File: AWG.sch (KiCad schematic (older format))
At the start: 83 parts, among them J1001 Conn_01x03, J1002 Conn_01x05, J1003 Conn_01x06, J1004 Conn_01x06, J2 Conn afficheur, J5 SMA, J6 SMA, J7 BNC, Q1001 NTE2633, Q1002 NTE2634, SW1 Reset, SW2 Encodeur sur façade, SW3 Next, SW4 Previous, SW5 AC/DC, SW6 50R/Low Z, U1 Pico, U1001 LM7812, U1002 L7912, U1003 LM7805, U1004 LM7905, U3 AD8055ARZ

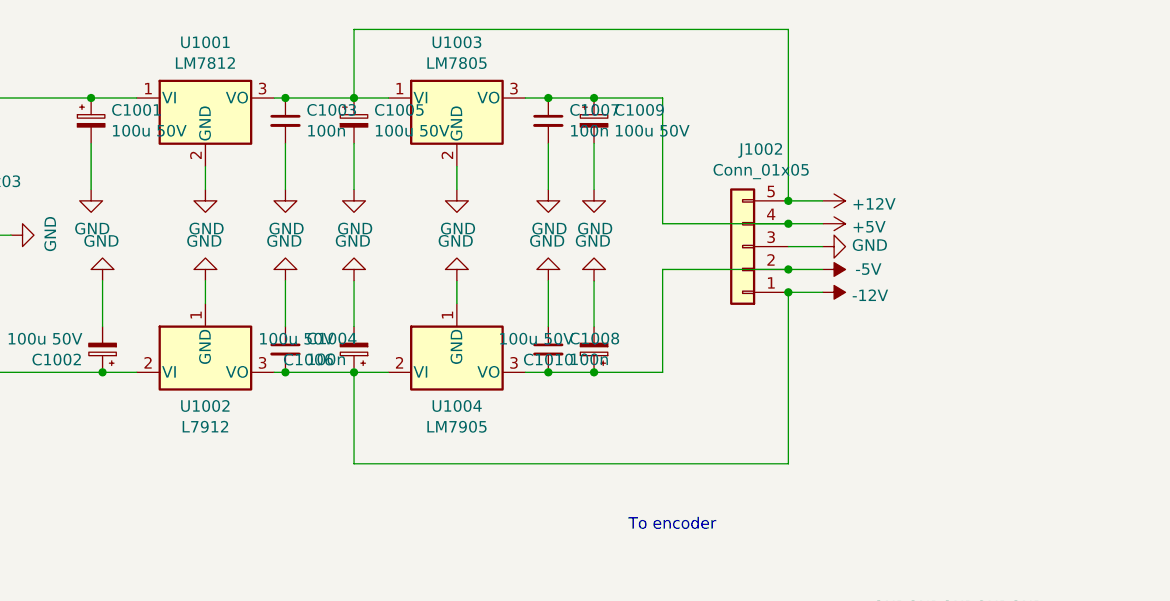
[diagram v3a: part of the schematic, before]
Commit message: D2Pack linear regulator added
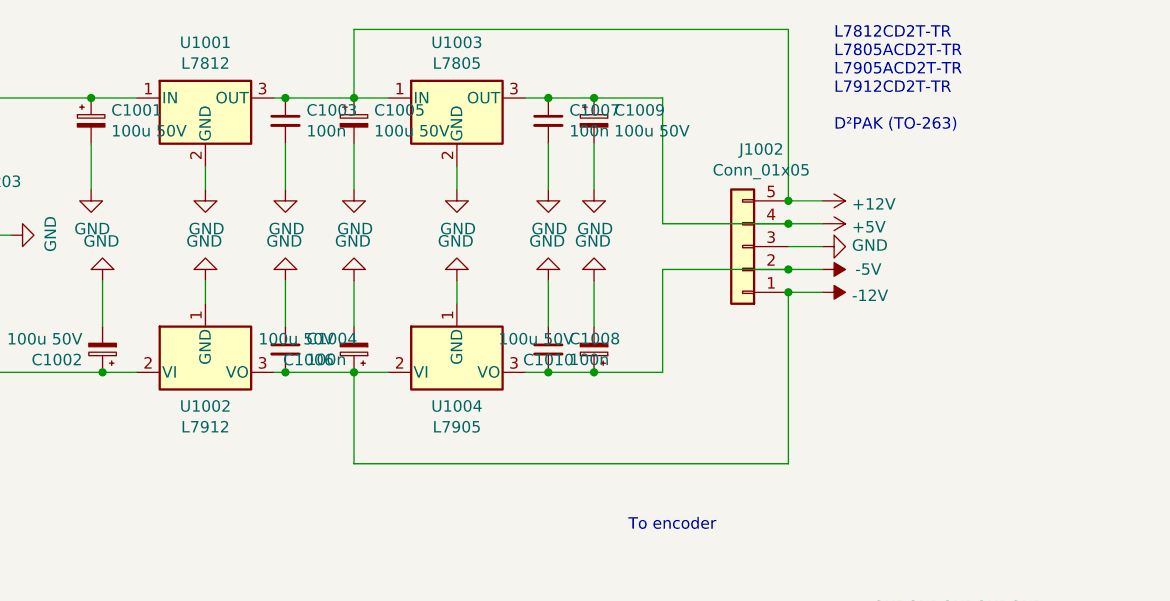
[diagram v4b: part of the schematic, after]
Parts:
- removed U1001: LM7812, Package_TO_SOT_THT:TO-220-3_Vertical, symbol Regulator_Linear:LM7812_TO220
- removed U1003: LM7805, Package_TO_SOT_THT:TO-220-3_Vertical, symbol Regulator_Linear:LM7805_TO220
- removed U1004: LM7905, Package_TO_SOT_THT:TO-220-3_Vertical, symbol Regulator_Linear:LM7905_TO220
- added U1001: L7812, Package_TO_SOT_SMD:TO-252-2, symbol Regulator_Linear:L7812
- added U1003: L7805, Package_TO_SOT_SMD:TO-252-2, symbol Regulator_Linear:L7805
- added U1004: L7905, Package_TO_SOT_SMD:TO-263-2, symbol Regulator_Linear:L7905
- U1002: footprint (none) -> Package_TO_SOT_SMD:TO-263-2
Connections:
- net +12V: now also U1001.3 (OUT), U1003.1 (IN)
- net +5V: now also U1003.3 (OUT)
- net -12V: now also U1004.2 (VI)
- net -5V: now also U1004.3 (VO)
- net GND: now also U1001.2 (GND), U1003.2 (GND), U1004.1 (GND)
- net at C1001.1, J1001.3 (Pin_3): now also U1001.1 (IN)
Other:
- note added: "L7812CD2T-TR\nL7805ACD2T-TR\nL7905ACD2T-TR\nL7912CD2T-TR\n\nD²PAK (TO-263)\n"
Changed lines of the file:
@@
-$EndComp
-$Comp
-L Regulator_Linear:LM7805_TO220 U1003
-U 1 1 61CB420E
-P 2800 850
-F 0 "U1003" H 2800 1092 50  0000 C CNN
-F 1 "LM7805" H 2800 1001 50  0000 C CNN
-F 2 "Package_TO_SOT_THT:TO-220-3_Vertical" H 2800 1075 50  0001 C CIN
-F 3 "https://www.onsemi.cn/PowerSolutions/document/MC7800-D.PDF" H 2800 800 50  0001 C CNN
-	1    2800 850
-	1    0    0    -1
-$EndComp
-$Comp
-L Regulator_Linear:LM7812_TO220 U1001
-U 1 1 61CB675E
-P 1700 850
-F 0 "U1001" H 1700 1092 50  0000 C CNN
-F 1 "LM7812" H 1700 1001 50  0000 C CNN
-F 2 "Package_TO_SOT_THT:TO-220-3_Vertical" H 1700 1075 50  0001 C CIN
-F 3 "https://www.onsemi.cn/PowerSolutions/document/MC7800-D.PDF" H 1700 800 50  0001 C CNN
-	1    1700 850
-	1    0    0    -1
-$EndComp
-$Comp
-L Regulator_Linear:LM7905_TO220 U1004
-U 1 1 61CB78CA
-P 2800 2050
-F 0 "U1004" H 2800 1901 50  0000 C CNN
-F 1 "LM7905" H 2800 1810 50  0000 C CNN
-F 2 "Package_TO_SOT_THT:TO-220-3_Vertical" H 2800 1850 50  0001 C CIN
-F 3 "https://www.onsemi.com/pub/Collateral/MC7900-D.PDF" H 2800 2050 50  0001 C CNN
-	1    2800 2050
-	1    0    0    -1
 $EndComp
 $Comp
@@
 F 0 "U1002" H 1700 1901 50  0000 C CNN
 F 1 "L7912" H 1700 1810 50  0000 C CNN
-F 2 "" H 1700 1850 50  0001 C CIN
+F 2 "Package_TO_SOT_SMD:TO-263-2" H 1700 1850 50  0001 C CIN
 F 3 "http://www.st.com/content/ccc/resource/technical/document/datasheet/c9/16/86/41/c7/2b/45/f2/CD00000450.pdf/files/CD00000450.pdf/jcr:content/translations/en.CD00000450.pdf" H 1700 2050 50  0001 C CNN
 	1    1700 2050
@@
 	1    0    0    1
 $EndComp
+Text Notes 4450 1000 0    50   ~ 0
+L7812CD2T-TR\nL7805ACD2T-TR\nL7905ACD2T-TR\nL7912CD2T-TR\n\nD²PAK (TO-263)\n
+$Comp
+L Regulator_Linear:L7905 U1004
+U 1 1 61D75CEB
+P 2800 2050
+F 0 "U1004" H 2800 1901 50  0000 C CNN
+F 1 "L7905" H 2800 1810 50  0000 C CNN
+F 2 "Package_TO_SOT_SMD:TO-263-2" H 2800 1850 50  0001 C CIN
+F 3 "http://www.st.com/content/ccc/resource/technical/document/datasheet/c9/16/86/41/c7/2b/45/f2/CD00000450.pdf/files/CD00000450.pdf/jcr:content/translations/en.CD00000450.pdf" H 2800 2050 50  0001 C CNN
+	1    2800 2050
+	1    0    0    -1
+$EndComp
+$Comp
+L Regulator_Linear:L7812 U1001
+U 1 1 61D77468
+P 1700 850
+F 0 "U1001" H 1700 1092 50  0000 C CNN
+F 1 "L7812" H 1700 1001 50  0000 C CNN
+F 2 "Package_TO_SOT_SMD:TO-252-2" H 1725 700 50  0001 L CIN
+F 3 "http://www.st.com/content/ccc/resource/technical/document/datasheet/41/4f/b3/b0/12/d4/47/88/CD00000444.pdf/files/CD00000444.pdf/jcr:content/translations/en.CD00000444.pdf" H 1700 800 50  0001 C CNN
+	1    1700 850
+	1    0    0    -1
+$EndComp
+$Comp
+L Regulator_Linear:L7805 U1003
+U 1 1 61D78CC9
+P 2800 850
+F 0 "U1003" H 2800 1092 50  0000 C CNN
+F 1 "L7805" H 2800 1001 50  0000 C CNN
+F 2 "Package_TO_SOT_SMD:TO-252-2" H 2825 700 50  0001 L CIN
+F 3 "http://www.st.com/content/ccc/resource/technical/document/datasheet/41/4f/b3/b0/12/d4/47/88/CD00000444.pdf/files/CD00000444.pdf/jcr:content/translations/en.CD00000444.pdf" H 2800 800 50  0001 C CNN
+	1    2800 850
+	1    0    0    -1
+$EndComp
 $EndSCHEMATC

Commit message: 3D shapes added
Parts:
- U1: footprint RPi_Pico:RPi_Pico_SMD_TH -> Pi_Pico:RPi_Pico_SMD_TH
- U1002, U1004: footprint Package_TO_SOT_SMD:TO-263-2 -> Package_TO_SOT_SMD:TO-252-2
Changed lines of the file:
@@
 F 0 "U1" H 3700 5723 50  0000 C CNN
 F 1 "Pico" H 3700 5814 50  0000 C CNN
-F 2 "RPi_Pico:RPi_Pico_SMD_TH" V 3700 4600 50  0001 C CNN
+F 2 "Pi_Pico:RPi_Pico_SMD_TH" V 3700 4600 50  0001 C CNN
 F 3 "" H 3700 4600 50  0001 C CNN
 	1    3700 4600
@@
 F 0 "U1002" H 1700 1901 50  0000 C CNN
 F 1 "L7912" H 1700 1810 50  0000 C CNN
-F 2 "Package_TO_SOT_SMD:TO-263-2" H 1700 1850 50  0001 C CIN
+F 2 "Package_TO_SOT_SMD:TO-252-2" H 1700 1850 50  0001 C CIN
 F 3 "http://www.st.com/content/ccc/resource/technical/document/datasheet/c9/16/86/41/c7/2b/45/f2/CD00000450.pdf/files/CD00000450.pdf/jcr:content/translations/en.CD00000450.pdf" H 1700 2050 50  0001 C CNN
 	1    1700 2050
@@
 F 0 "U1004" H 2800 1901 50  0000 C CNN
 F 1 "L7905" H 2800 1810 50  0000 C CNN
-F 2 "Package_TO_SOT_SMD:TO-263-2" H 2800 1850 50  0001 C CIN
+F 2 "Package_TO_SOT_SMD:TO-252-2" H 2800 1850 50  0001 C CIN
 F 3 "http://www.st.com/content/ccc/resource/technical/document/datasheet/c9/16/86/41/c7/2b/45/f2/CD00000450.pdf/files/CD00000450.pdf/jcr:content/translations/en.CD00000450.pdf" H 2800 2050 50  0001 C CNN
 	1    2800 2050

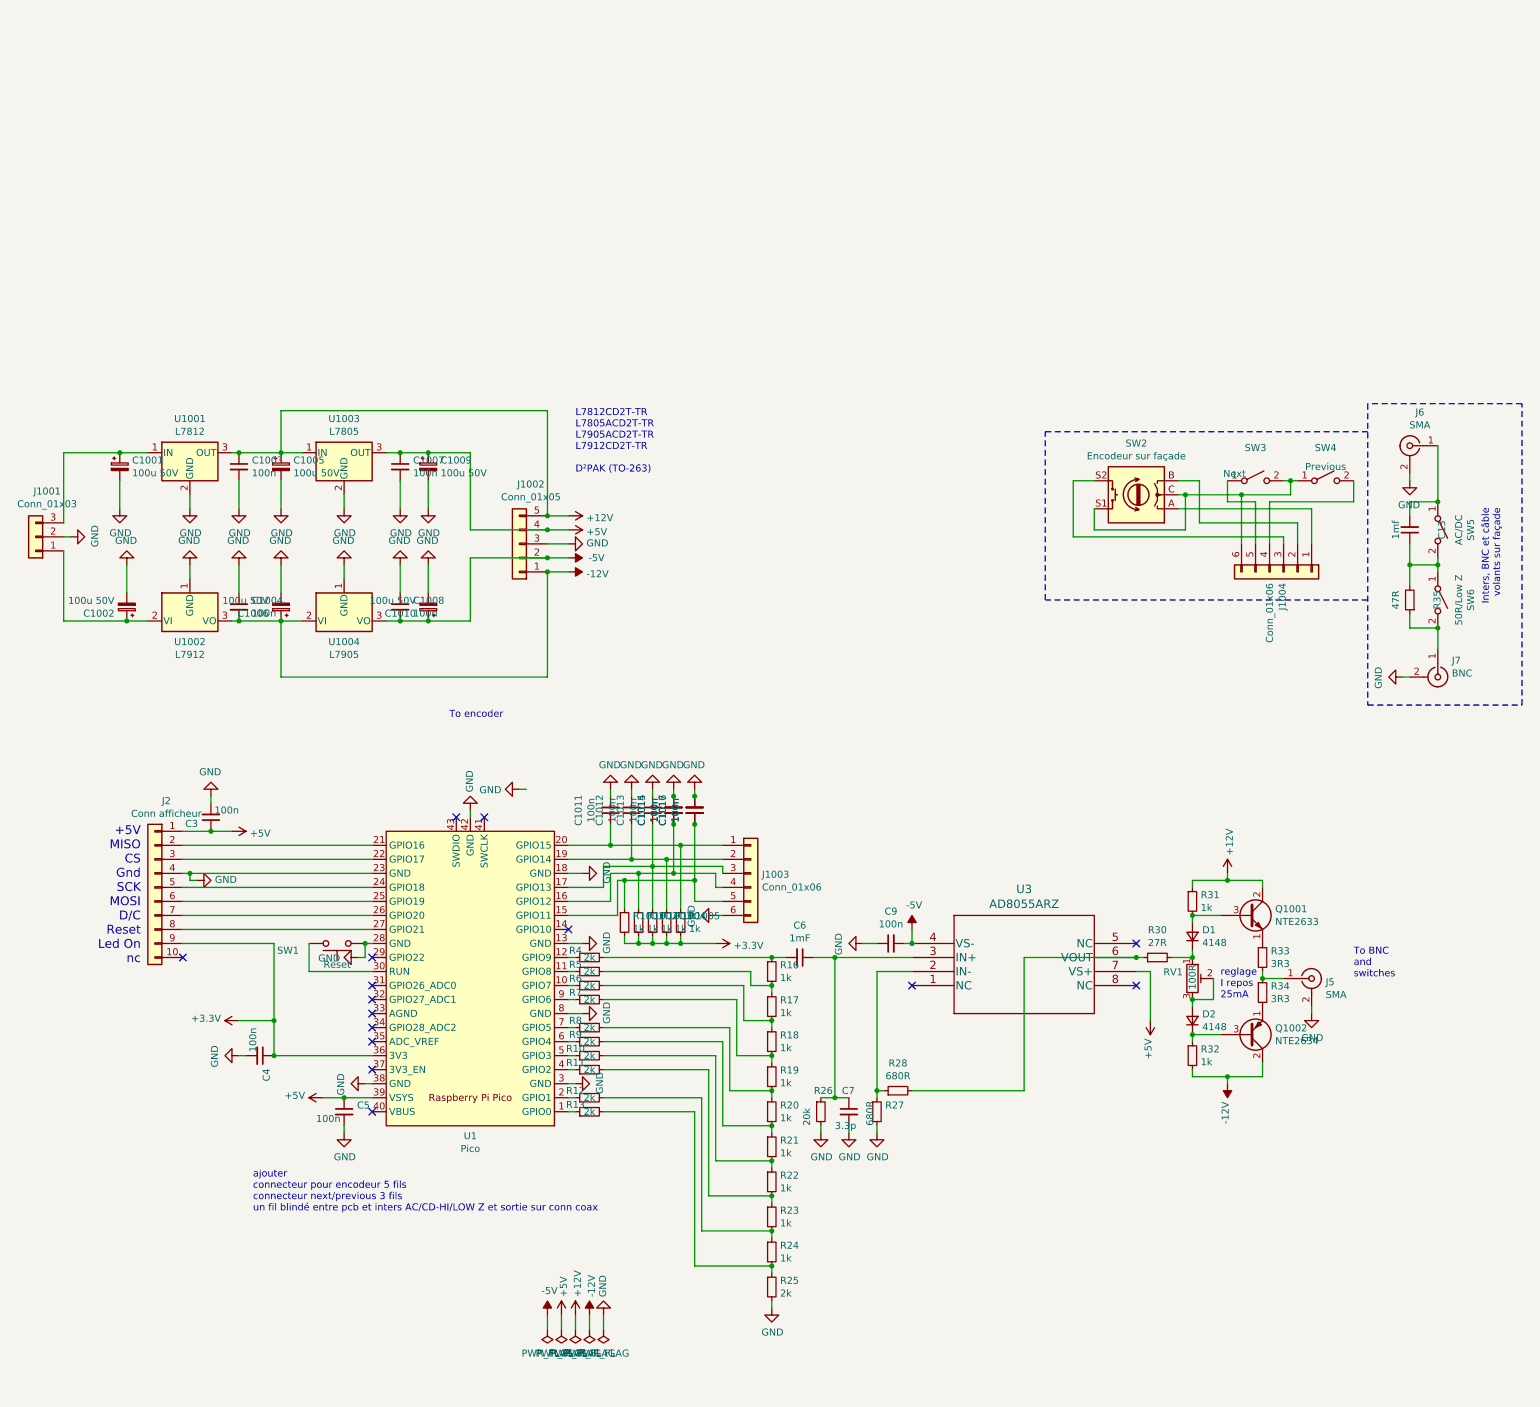
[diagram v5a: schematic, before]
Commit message: heatsink added
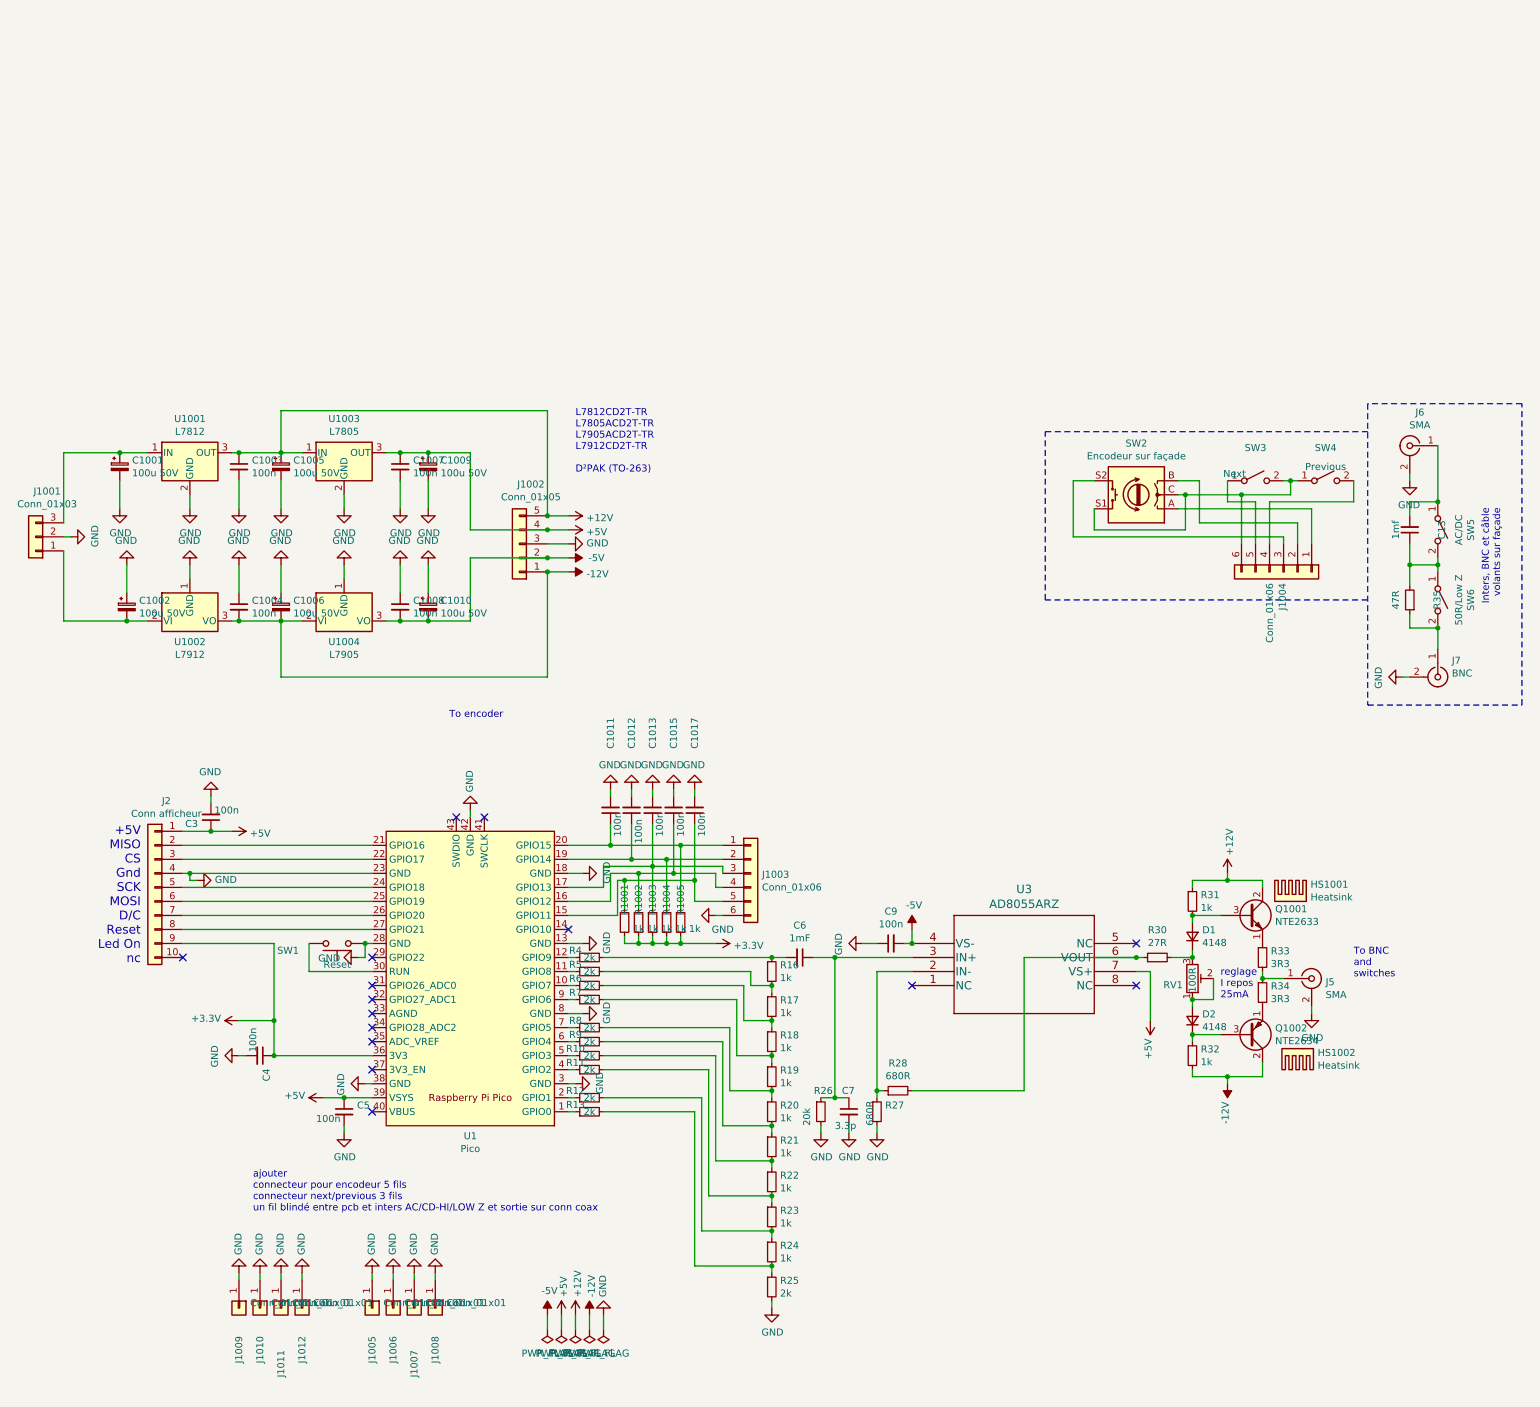
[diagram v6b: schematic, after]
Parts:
- removed C1014, C1016: 100n, Capacitor_SMD:C_0805_2012Metric_Pad1.18x1.45mm_HandSolder, symbol Device:C_Small
- added HS1001, HS1002: Heatsink, Heatsink:Heatsink_Aavid-TV5G_TO220_Horizontal, symbol Mechanical:Heatsink
- added J1005, J1006, J1007, J1008, J1009, J1010, J1011, J1012: Conn_01x01, MountingHole:MountingHole_3.2mm_M3_Pad_Via, symbol Connector_Generic:Conn_01x01
- D1, D2: footprint Diode_SMD:D_MELF_Handsoldering -> Diode_SMD:D_MiniMELF_Handsoldering
- J1004: footprint Connector_Molex:Molex_KK-254_AE-6410-06A_1x06_P2.54mm_Vertical -> (none)
- J6: footprint SMA_PINS:SMA_EDGE_NRW -> (none)
- R35: footprint Resistor_SMD:R_0603_1608Metric_Pad0.98x0.95mm_HandSolder -> (none)
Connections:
- net -12V: now also C1006.2; no longer C1006.1
- net -5V: now also C1010.2; no longer C1010.1
- net GND: now also C1002.1, C1006.1, C1010.1, J1005.1 (Pin_1), J1006.1 (Pin_1), J1007.1 (Pin_1), J1008.1 (Pin_1), J1009.1 (Pin_1), J1010.1 (Pin_1), J1011.1 (Pin_1), J1012.1 (Pin_1); no longer C1002.2, C1006.2, C1010.2
- net at D1.1 (K), R30.2: now also RV1.3; no longer RV1.1
- net at D2.2 (A), RV1.2: now also RV1.1; no longer RV1.3
- net at J1001.1 (Pin_1), U1002.2 (VI): now also C1002.2; no longer C1002.1
